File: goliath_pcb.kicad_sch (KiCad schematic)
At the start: 91 parts, among them IC1 MCT9001SD, IC2 MCT9001SD, IC3 MCT9001SD, IC4 MCT9001SD, IC5 MCT9001SD, IC6 MCT9001SD, IC7 MCT9001SD, J1 RJ45_LED, J10 Conn_01x04_Male, J11 Screw_Terminal_01x02, J12 Screw_Terminal_01x02, J13 Screw_Terminal_01x02, J2 RJ45_LED, J3 RJ45_LED, J4 RJ45_LED, J5 Conn_01x08_Male, J6 Conn_01x08_Male, J7 Conn_01x02_Male, J8 Conn_01x04_Male, J9 Conn_01x04_Male, Q1 STP2N80K5, Q2 STP2N80K5, U1 Pico, U2 LM2592HVT-5.0/NOPB, U3 74HCT244, U4 74HCT244, U5 MCP3008, U6 PCF8574, U7 PCF8574

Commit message: Actually connect MOSFETs to logic outputs
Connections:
- net GND: no longer U4.11 (2A3), U4.13 (2A2)
- net at J5.1 (Pin_1), U6.4 (P0): now also U4.13 (2A2)
- net at J5.2 (Pin_2), U6.5 (P1): now also U4.11 (2A3)
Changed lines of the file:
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@@
   (junction (at 116.84 238.76) (diameter 0) (color 0 0 0 0)
   )
+  (junction (at 81.28 176.53) (diameter 0) (color 0 0 0 0)
+  )
   (junction (at 304.8 217.17) (diameter 0) (color 0 0 0 0)
   )
@@
   (junction (at 162.56 185.42) (diameter 0) (color 0 0 0 0)
   )
+  (junction (at 81.28 179.07) (diameter 0) (color 0 0 0 0)
+  )
   (junction (at 213.36 52.07) (diameter 0) (color 0 0 0 0)
   )
@@
     (stroke (width 0) (type default) (color 0 0 0 0))
   )
+  (wire (pts (xy 96.52 148.59) (xy 114.3 148.59))
+    (stroke (width 0) (type default) (color 0 0 0 0))
+  )
   (wire (pts (xy 96.52 34.29) (xy 96.52 52.07))
     (stroke (width 0) (type default) (color 0 0 0 0))
@@
     (stroke (width 0) (type default) (color 0 0 0 0))
   )
+  (wire (pts (xy 81.28 179.07) (xy 96.52 179.07))
+    (stroke (width 0) (type default) (color 0 0 0 0))
+  )
   (wire (pts (xy 38.1 177.8) (xy 45.72 177.8))
     (stroke (width 0) (type default) (color 0 0 0 0))
@@
     (stroke (width 0) (type default) (color 0 0 0 0))
   )
+  (wire (pts (xy 96.52 179.07) (xy 96.52 148.59))
+    (stroke (width 0) (type default) (color 0 0 0 0))
+  )
   (wire (pts (xy 25.4 138.43) (xy 25.4 77.47))
     (stroke (width 0) (type default) (color 0 0 0 0))
@@
     (stroke (width 0) (type default) (color 0 0 0 0))
   )
+  (wire (pts (xy 81.28 176.53) (xy 95.25 176.53))
+    (stroke (width 0) (type default) (color 0 0 0 0))
+  )
   (wire (pts (xy 71.12 227.33) (xy 81.28 227.33))
     (stroke (width 0) (type default) (color 0 0 0 0))
@@
     (stroke (width 0) (type default) (color 0 0 0 0))
   )
+  (wire (pts (xy 95.25 176.53) (xy 95.25 146.05))
+    (stroke (width 0) (type default) (color 0 0 0 0))
+  )
   (wire (pts (xy 147.32 110.49) (xy 154.94 110.49))
     (stroke (width 0) (type default) (color 0 0 0 0))
@@
     (stroke (width 0) (type default) (color 0 0 0 0))
   )
+  (wire (pts (xy 95.25 146.05) (xy 114.3 146.05))
+    (stroke (width 0) (type default) (color 0 0 0 0))
+  )
   (wire (pts (xy 316.23 207.01) (xy 308.61 207.01))
     (stroke (width 0) (type default) (color 0 0 0 0))
@@
     (pin "1")
   )
-  (symbol (lib_id "power:GND") (at 114.3 148.59 270) (unit 1)
-    (in_bom yes) (on_board yes)
-    (property "Reference" "#PWR021" (id 0) (at 107.95 148.59 0)
-      (effects (font (size 1.27 1.27)) hide)
-    )
-    (property "Value" "GND" (id 1) (at 106.68 148.59 90)
-      (effects (font (size 1.27 1.27)) (justify left))
-    )
-    (property "Footprint" "" (id 2) (at 114.3 148.59 0)
-      (effects (font (size 1.27 1.27)) hide)
-    )
-    (property "Datasheet" "" (id 3) (at 114.3 148.59 0)
-      (effects (font (size 1.27 1.27)) hide)
-    )
-    (pin "1")
-  )
   (symbol (lib_id "STP2N80K5:STP2N80K5") (at 274.32 204.47 0) (unit 1)
     (in_bom yes) (on_board yes)
@@
     (pin "4")
   )
-  (symbol (lib_id "power:GND") (at 114.3 146.05 270) (unit 1)
-    (in_bom yes) (on_board yes)
-    (property "Reference" "#PWR020" (id 0) (at 107.95 146.05 0)
-      (effects (font (size 1.27 1.27)) hide)
-    )
-    (property "Value" "GND" (id 1) (at 106.68 146.05 90)
-      (effects (font (size 1.27 1.27)) (justify left))
-    )
-    (property "Footprint" "" (id 2) (at 114.3 146.05 0)
-      (effects (font (size 1.27 1.27)) hide)
-    )
-    (property "Datasheet" "" (id 3) (at 114.3 146.05 0)
-      (effects (font (size 1.27 1.27)) hide)
-    )
-    (pin "1")
-  )
   (symbol (lib_id "power:GND") (at 363.22 162.56 270) (unit 1)
     (in_bom yes) (on_board yes)
@@
       (reference "#PWR019") (unit 1) (value "GND") (footprint "")
     )
-    (path "/5e0b0b15-b0bd-4201-83d8-f32f24ed1580"
-      (reference "#PWR020") (unit 1) (value "GND") (footprint "")
-    )
-    (path "/50b14f6b-fab4-4649-ac15-bfe6be0d8a2a"
-      (reference "#PWR021") (unit 1) (value "GND") (footprint "")
-    )
     (path "/822e0d65-d415-4a22-8e32-d018d0fee0fd"

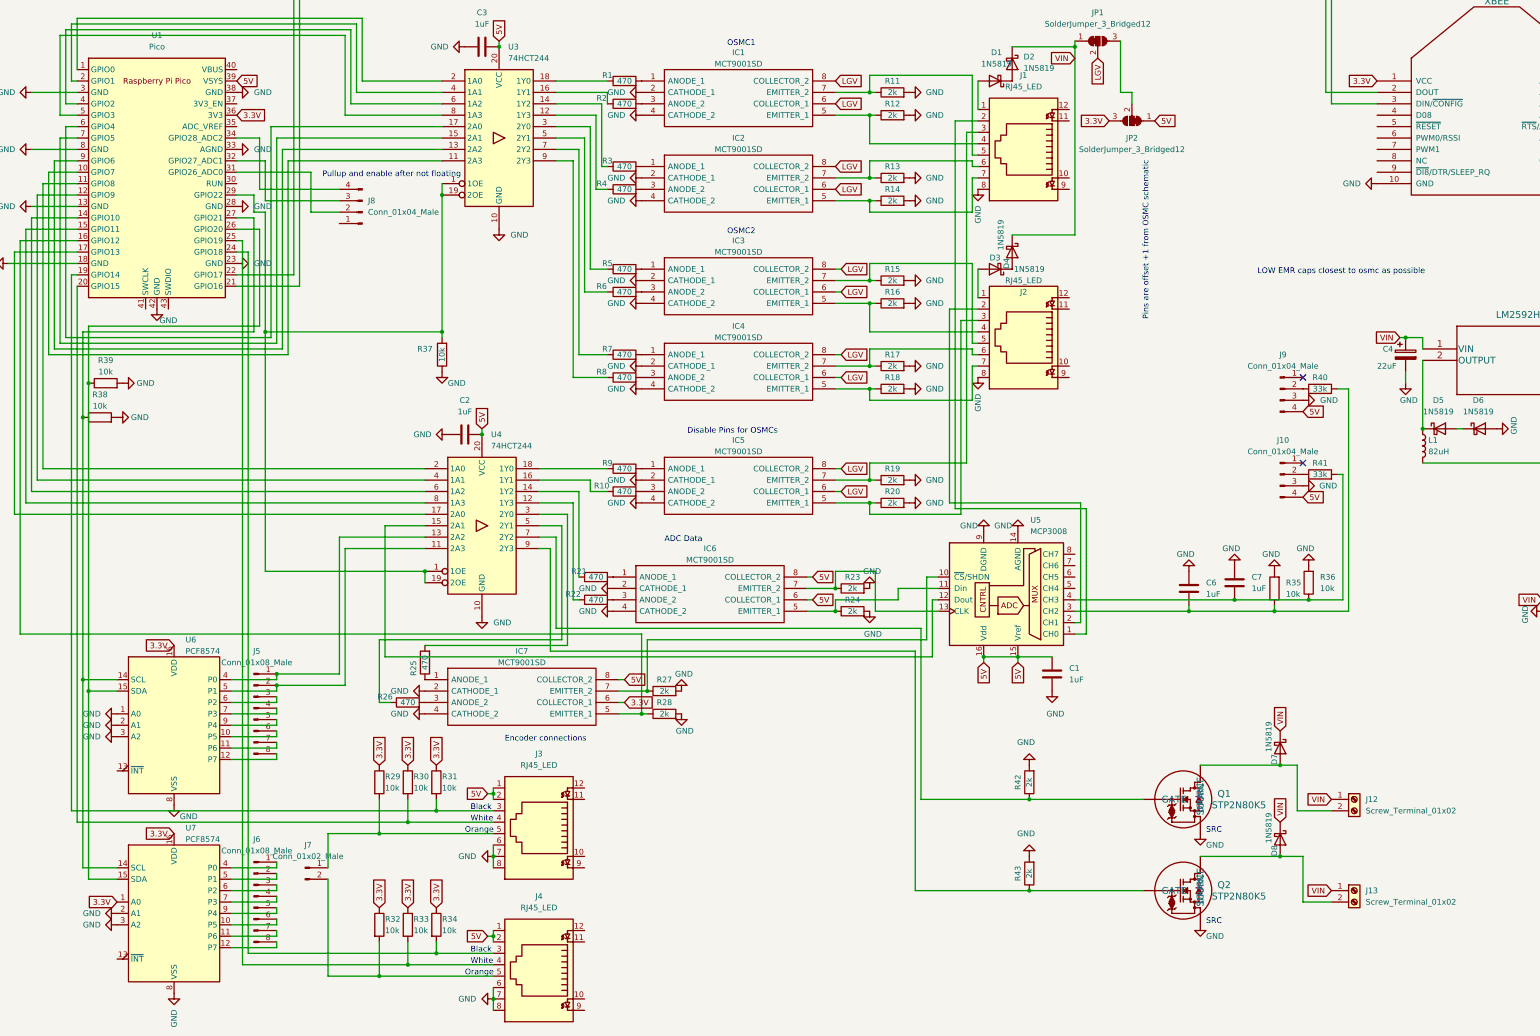
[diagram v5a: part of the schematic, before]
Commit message: Add comments via silkscreen, start to use alternative kicad library
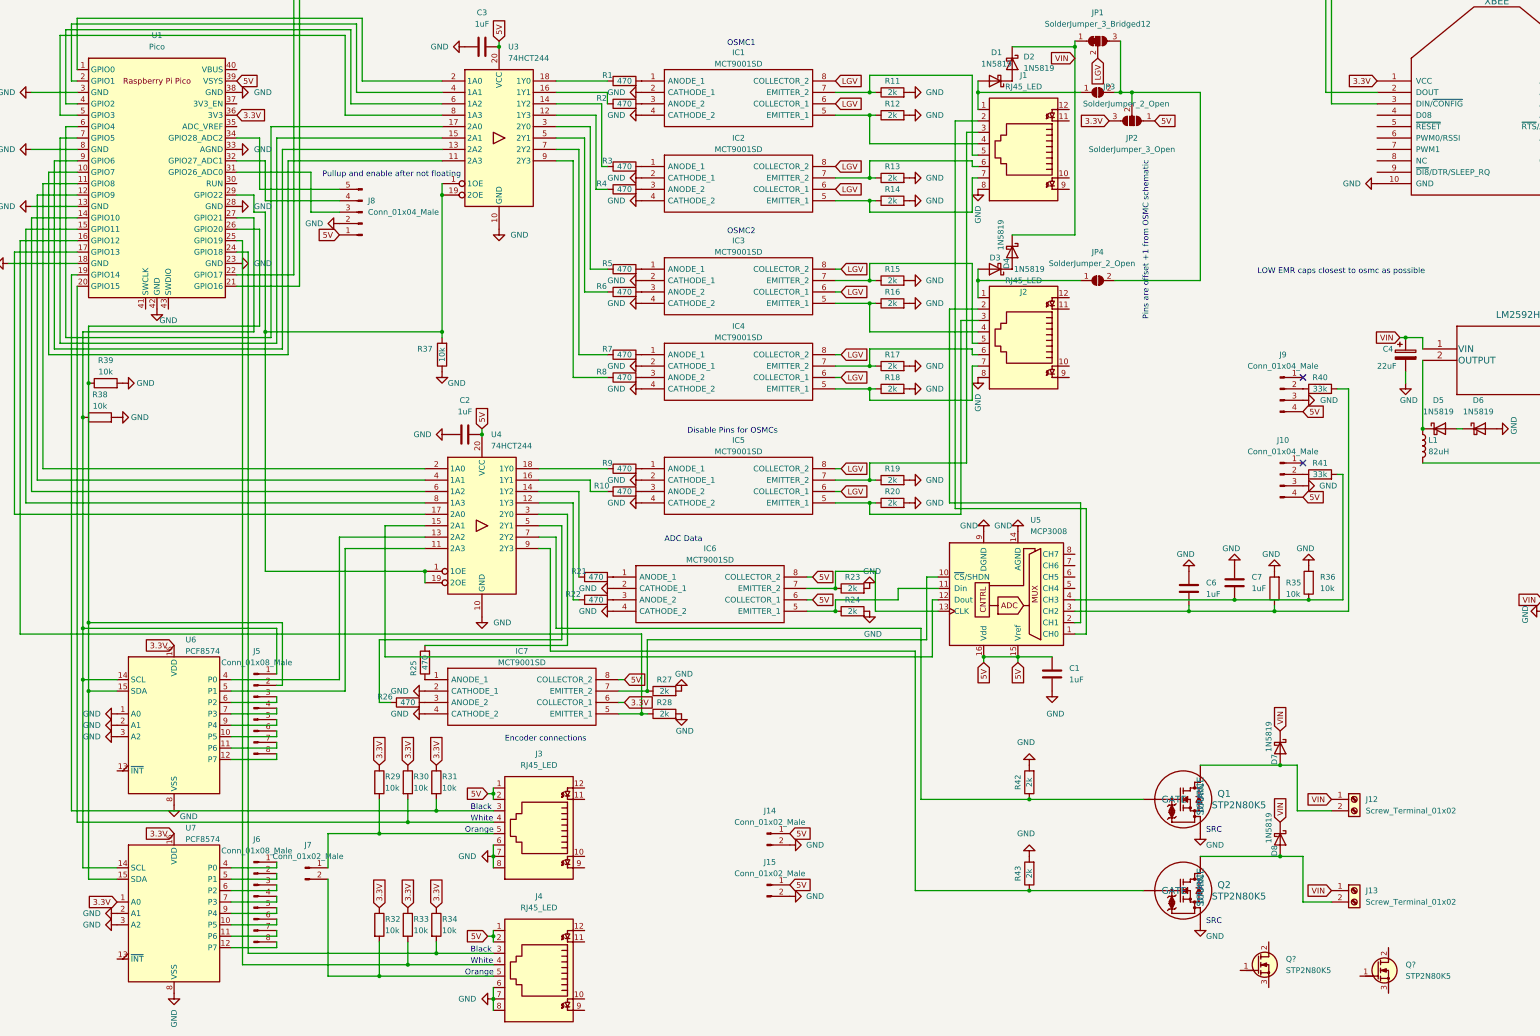
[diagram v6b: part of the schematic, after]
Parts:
- removed JP2: SolderJumper_3_Bridged12, Jumper:SolderJumper-3_P1.3mm_Open_Pad1.0x1.5mm, symbol Jumper:SolderJumper_3_Bridged12
- added J14, J15: Conn_01x02_Male, Connector_PinHeader_2.54mm:PinHeader_1x02_P2.54mm_Vertical, symbol Connector:Conn_01x02_Male
- added JP2: SolderJumper_3_Open, Jumper:SolderJumper-3_P1.3mm_Open_Pad1.0x1.5mm, symbol Jumper:SolderJumper_3_Open
- added JP3, JP4: SolderJumper_2_Open, Jumper:SolderJumper-2_P1.3mm_Open_Pad1.0x1.5mm, symbol Jumper:SolderJumper_2_Open
- added Q? (x2): STP2N80K5, Package_TO_SOT_THT_AKL:TO-220-3_Vertical_GDS, symbol Transistor_MOSFET_AKL:STP2N80K5
- J8: footprint Connector_PinHeader_2.54mm:PinHeader_1x04_P2.54mm_Vertical -> Connector_PinHeader_2.54mm:PinHeader_1x05_P2.54mm_Vertical; symbol Connector:Conn_01x04_Male -> Connector:Conn_01x05_Male
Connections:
- net 3.3V: now also JP2.3 (B)
- net 5V: now also J8.1 (Pin_1), J14.1 (Pin_1), J15.1 (Pin_1), JP2.1 (A)
- net GND: now also J8.2 (Pin_2), J14.2 (Pin_2), J15.2 (Pin_2)
- net at D1.2 (A), J1.1: now also JP3.1 (A)
- net at D3.2 (A), J2.1: now also JP4.1 (A)
- net at JP1.3 (B): now also JP2.2 (C), JP3.2 (B), JP4.2 (B)
- net at R38.1, U1.27 (GPIO21), U6.14 (SCL)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: now also J5.1 (Pin_1)
- net at R39.1, U1.26 (GPIO20), U6.15 (SDA)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: now also J5.2 (Pin_2)
- net at U4.11 (2A3), U6.5 (P1): no longer J5.2 (Pin_2)
- net at U4.13 (2A2), U6.4 (P0): no longer J5.1 (Pin_1)
- net at U1.31 (GPIO26_ADC0): now also J8.3 (Pin_3); no longer J8.2 (Pin_2)
- net at U1.32 (GPIO27_ADC1): now also J8.4 (Pin_4); no longer J8.3 (Pin_3)
- net at U1.34 (GPIO28_ADC2): now also J8.5 (Pin_5); no longer J8.4 (Pin_4)

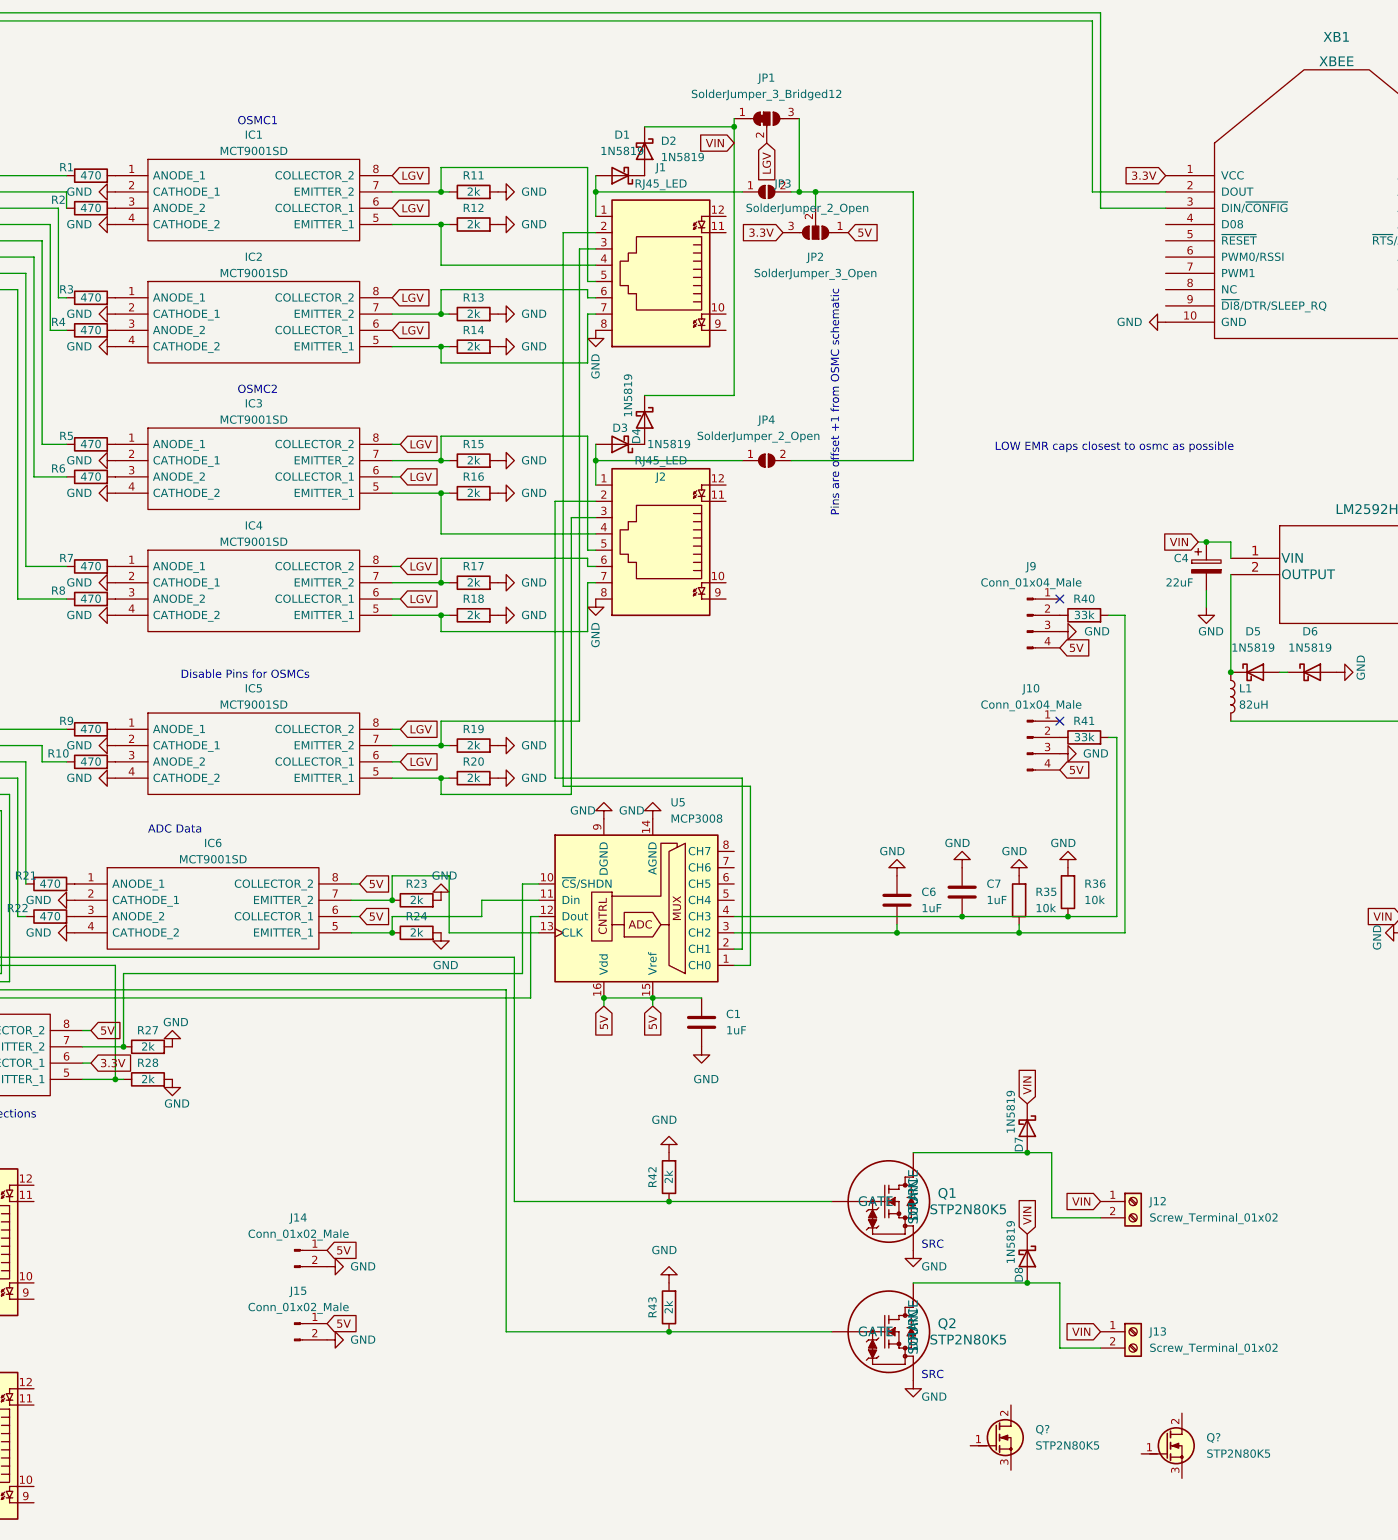
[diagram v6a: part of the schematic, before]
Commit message: Add some symbol replacements
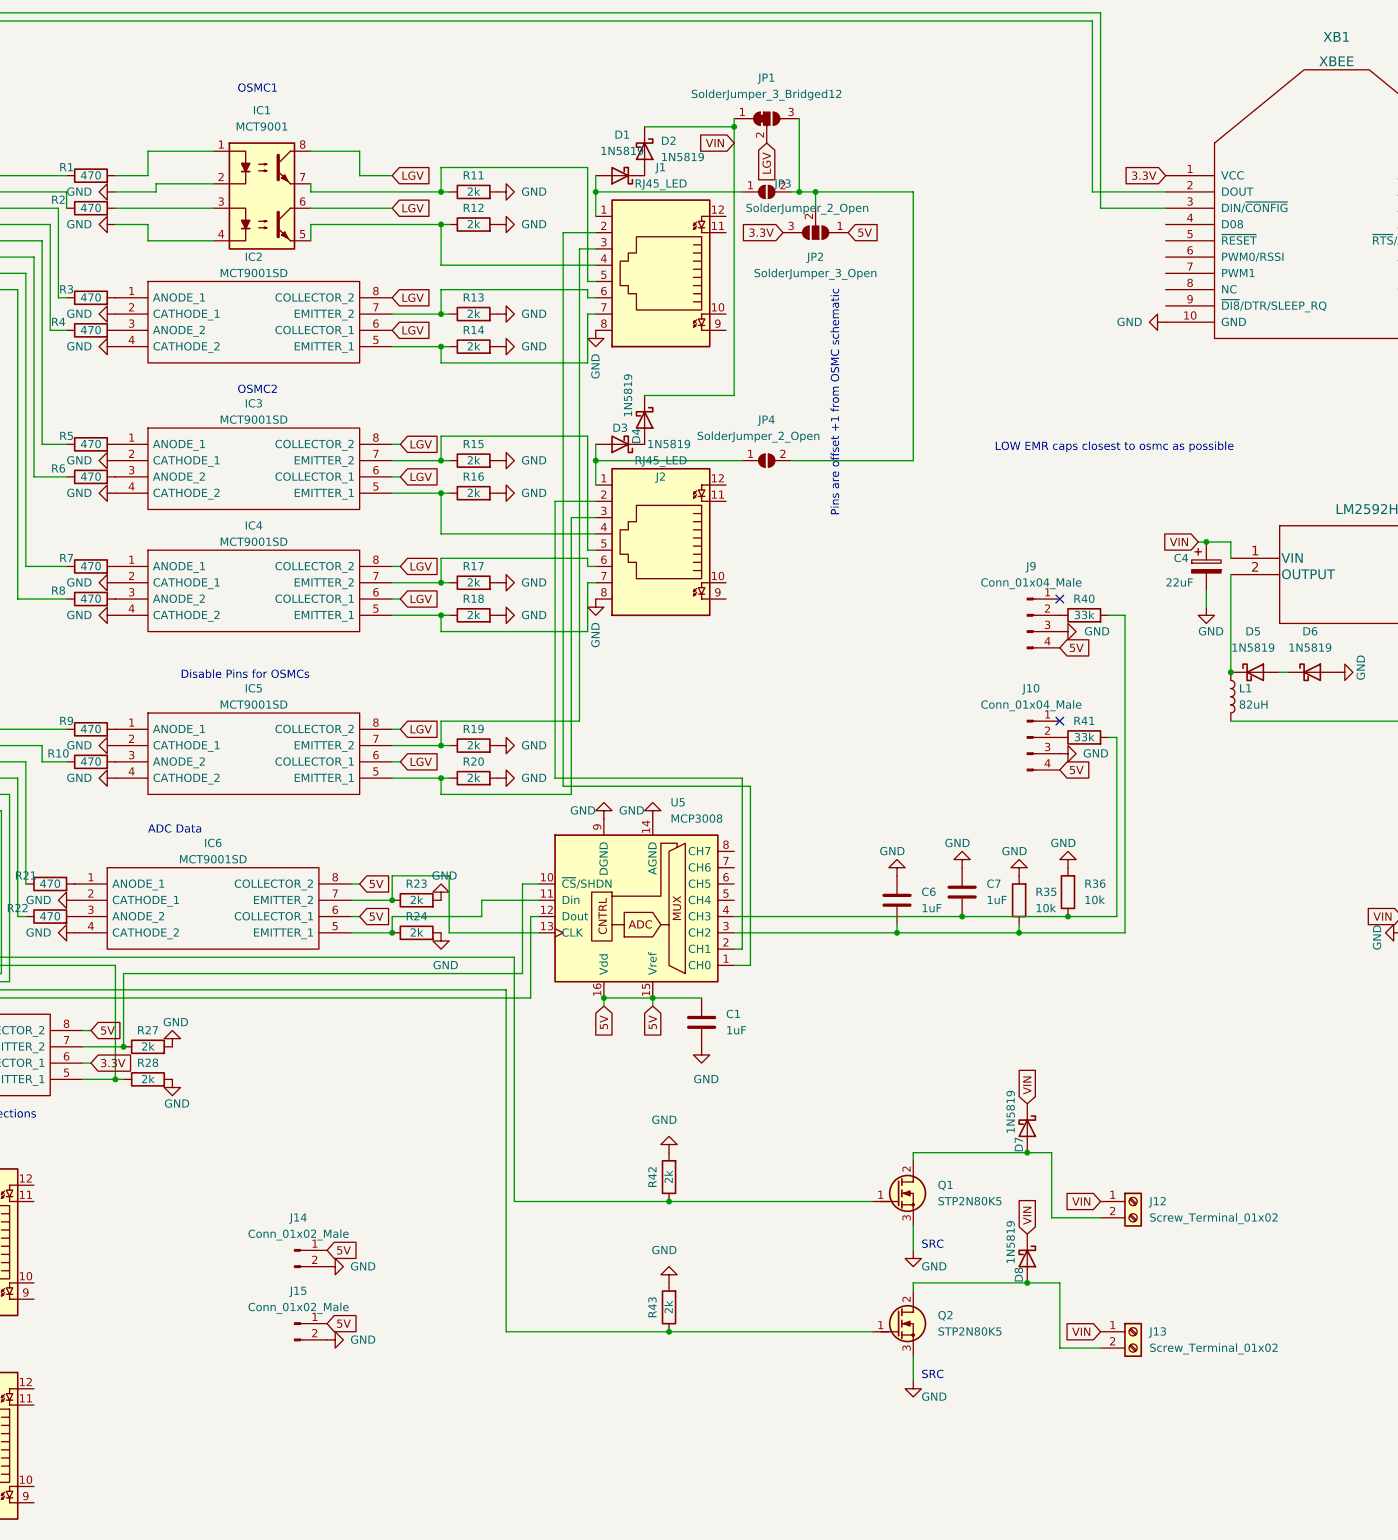
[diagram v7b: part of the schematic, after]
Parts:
- removed IC1: MCT9001SD, Package_DIP:DIP-8_W7.62mm_Socket, symbol MCT9001SD:MCT9001SD
- removed Q1, Q2: STP2N80K5, STP2N80K5:STP2N80K5, symbol STP2N80K5:STP2N80K5
- added IC1: MCT9001, Package_DIP:DIP-8_W7.62mm_Socket, symbol Optocoupler_AKL:MCT9001
- gave numbers to parts that had none: 2
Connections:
- net GND: now also Q1.3 (S), Q2.3 (S), IC1.2, IC1.4
- net LGV: now also IC1.6, IC1.8
- net at Q1.1 (G): now also R42.1, U4.7 (2Y2)
- net at Q1.2 (D): now also D7.2 (A), J12.2 (Pin_2)
- net at D8.2 (A), J13.2 (Pin_2): now also Q2.2 (D)
- net at R1.2: now also IC1.1
- net at J1.4, R12.1: now also IC1.5
- net at J1.5, R11.1: now also IC1.7
- net at R43.1, U4.9 (2Y3): now also Q2.1 (G)
- net at R2.2: now also IC1.3
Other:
- moved on the sheet: Q1, Q2
